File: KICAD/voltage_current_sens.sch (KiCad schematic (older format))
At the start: 4 parts

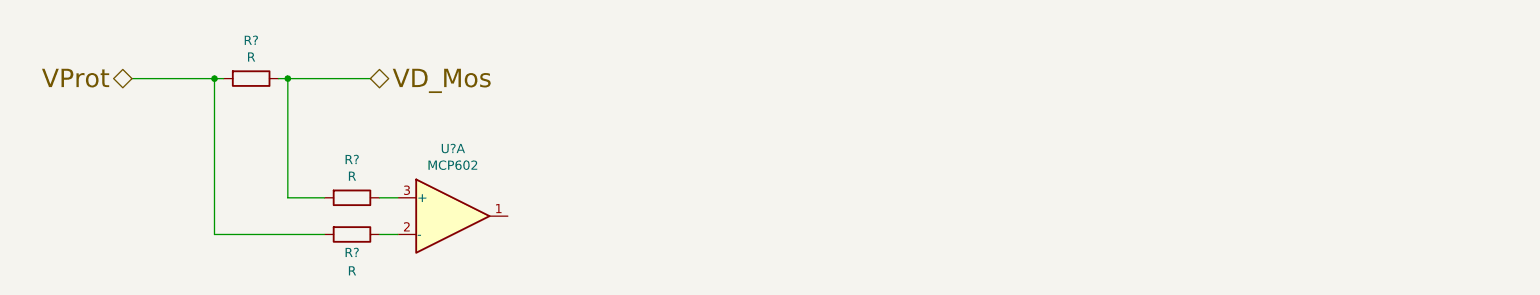
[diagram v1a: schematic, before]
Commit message: labels dans les blocks
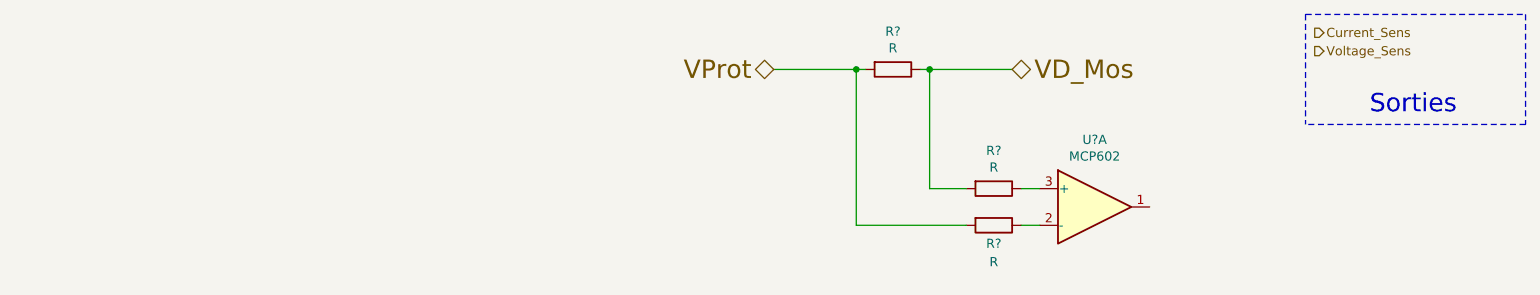
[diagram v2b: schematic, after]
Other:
- note added: "Sorties"
- moved on the sheet: R?, U?A
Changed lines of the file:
@@
 $Descr A4 11693 8268
 encoding utf-8
-Sheet 12 15
+Sheet 3 15
 Title "SESAME"
 Date ""
@@
 Comment4 ""
 $EndDescr
-Text HLabel 3350 3100 2    100  BiDi ~ 0
+Text HLabel 6850 3050 2    100  BiDi ~ 0
 VD_Mos
-Text HLabel 2050 3100 0    100  BiDi ~ 0
+Text HLabel 5550 3050 0    100  BiDi ~ 0
 VProt
 Wire Wire Line
-	2550 3100 2500 3100
+	6050 3050 6000 3050
 Wire Wire Line
-	2850 3100 2900 3100
+	6350 3050 6400 3050
 Wire Wire Line
-	3400 3750 3500 3750
+	6900 3700 7000 3700
 Wire Wire Line
-	3400 3950 3500 3950
+	6900 3900 7000 3900
 Wire Wire Line
-	3100 3750 2900 3750
+	6600 3700 6400 3700
 Wire Wire Line
-	2900 3750 2900 3100
-Connection ~ 2900 3100
+	6400 3700 6400 3050
+Connection ~ 6400 3050
 Wire Wire Line
-	2900 3100 3350 3100
+	6400 3050 6850 3050
 Wire Wire Line
-	2500 3100 2500 3950
+	6000 3050 6000 3900
 Wire Wire Line
-	2500 3950 3100 3950
-Connection ~ 2500 3100
+	6000 3900 6600 3900
+Connection ~ 6000 3050
 Wire Wire Line
-	2500 3100 2050 3100
+	6000 3050 5550 3050
 $Comp
 L Device:R R?
 U 1 1 6109114F
-P 2700 3100
+P 6200 3050
 AR Path="/60F19D5B/6109114F" Ref="R?"  Part="1"
 AR Path="/60F171CE/6109114F" Ref="R?"  Part="1"
-F 0 "R?" V 2493 3100 50  0000 C CNN
-F 1 "R" V 2584 3100 50  0000 C CNN
-F 2 "" V 2630 3100 50  0001 C CNN
-F 3 "~" H 2700 3100 50  0001 C CNN
-	1    2700 3100
+F 0 "R?" V 5993 3050 50  0000 C CNN
+F 1 "R" V 6084 3050 50  0000 C CNN
+F 2 "" V 6130 3050 50  0001 C CNN
+F 3 "~" H 6200 3050 50  0001 C CNN
+	1    6200 3050
 	0    1    1    0
 $EndComp
@@
 L Device:R R?
 U 1 1 61091B7C
-P 3250 3950
+P 6750 3900
 AR Path="/60F19D5B/61091B7C" Ref="R?"  Part="1"
 AR Path="/60F171CE/61091B7C" Ref="R?"  Part="1"
-F 0 "R?" V 3350 3950 50  0000 C CNN
-F 1 "R" V 3450 3950 50  0000 C CNN
-F 2 "" V 3180 3950 50  0001 C CNN
-F 3 "~" H 3250 3950 50  0001 C CNN
-	1    3250 3950
+F 0 "R?" V 6850 3900 50  0000 C CNN
+F 1 "R" V 6950 3900 50  0000 C CNN
+F 2 "" V 6680 3900 50  0001 C CNN
+F 3 "~" H 6750 3900 50  0001 C CNN
+	1    6750 3900
 	0    1    1    0
 $EndComp
@@
 L Device:R R?
 U 1 1 610923D6
-P 3250 3750
+P 6750 3700
 AR Path="/60F19D5B/610923D6" Ref="R?"  Part="1"
 AR Path="/60F171CE/610923D6" Ref="R?"  Part="1"
-F 0 "R?" V 3043 3750 50  0000 C CNN
-F 1 "R" V 3134 3750 50  0000 C CNN
-F 2 "" V 3180 3750 50  0001 C CNN
-F 3 "~" H 3250 3750 50  0001 C CNN
-	1    3250 3750
+F 0 "R?" V 6543 3700 50  0000 C CNN
+F 1 "R" V 6634 3700 50  0000 C CNN
+F 2 "" V 6680 3700 50  0001 C CNN
+F 3 "~" H 6750 3700 50  0001 C CNN
+	1    6750 3700
 	0    1    1    0
 $EndComp
@@
 L Amplifier_Operational:MCP602 U?
 U 1 1 61093F22
-P 3800 3850
+P 7300 3800
 AR Path="/60F19D5B/61093F22" Ref="U?"  Part="1"
 AR Path="/60F171CE/61093F22" Ref="U?"  Part="1"
-F 0 "U?" H 3800 4217 50  0000 C CNN
-F 1 "MCP602" H 3800 4126 50  0000 C CNN
-F 2 "" H 3800 3850 50  0001 C CNN
-F 3 "http://ww1.microchip.com/downloads/en/DeviceDoc/21314g.pdf" H 3800 3850 50  0001 C CNN
-	1    3800 3850
+F 0 "U?" H 7300 4167 50  0000 C CNN
+F 1 "MCP602" H 7300 4076 50  0000 C CNN
+F 2 "" H 7300 3800 50  0001 C CNN
+F 3 "http://ww1.microchip.com/downloads/en/DeviceDoc/21314g.pdf" H 7300 3800 50  0001 C CNN
+	1    7300 3800
 	1    0    0    -1
 $EndComp
+Text HLabel 8500 2850 2    50   Output ~ 0
+Current_Sens
+Text HLabel 8500 2950 2    50   Output ~ 0
+Voltage_Sens
+Wire Notes Line
+	8450 2750 9650 2750
+Wire Notes Line
+	9650 2750 9650 3350
+Wire Notes Line
+	9650 3350 8450 3350
+Wire Notes Line
+	8450 2750 8450 3350
+Text Notes 8800 3300 0    100  ~ 0
+Sorties
 $EndSCHEMATC

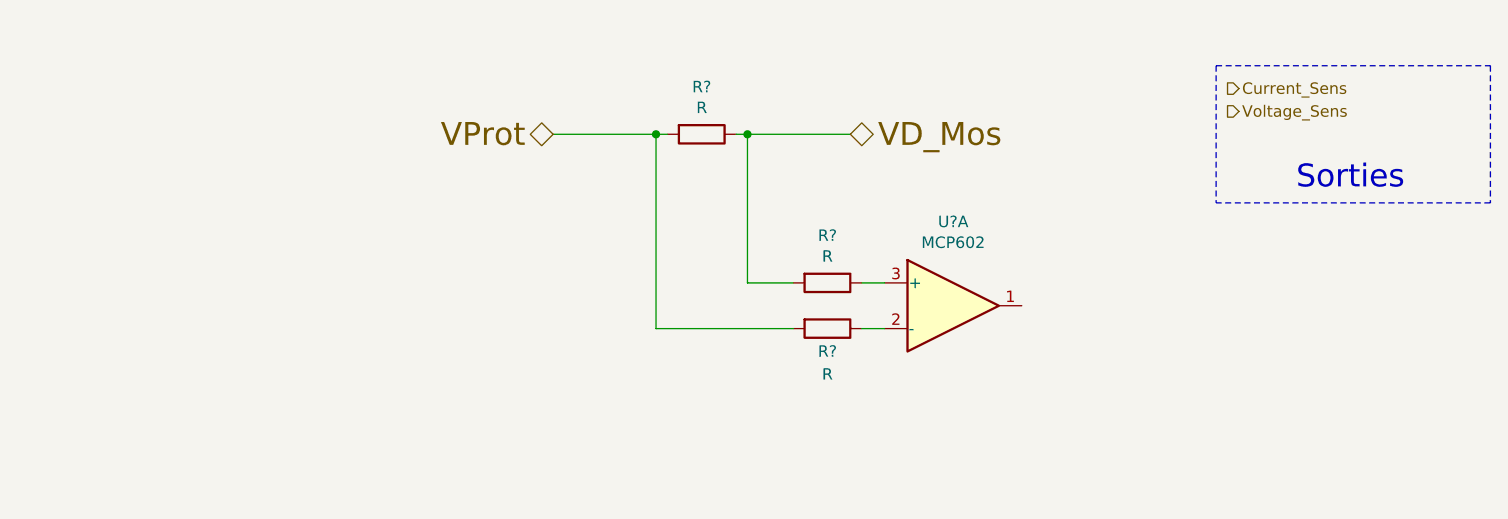
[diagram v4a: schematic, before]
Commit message: added ina240 sim + drawed protect and DC-DC chopper
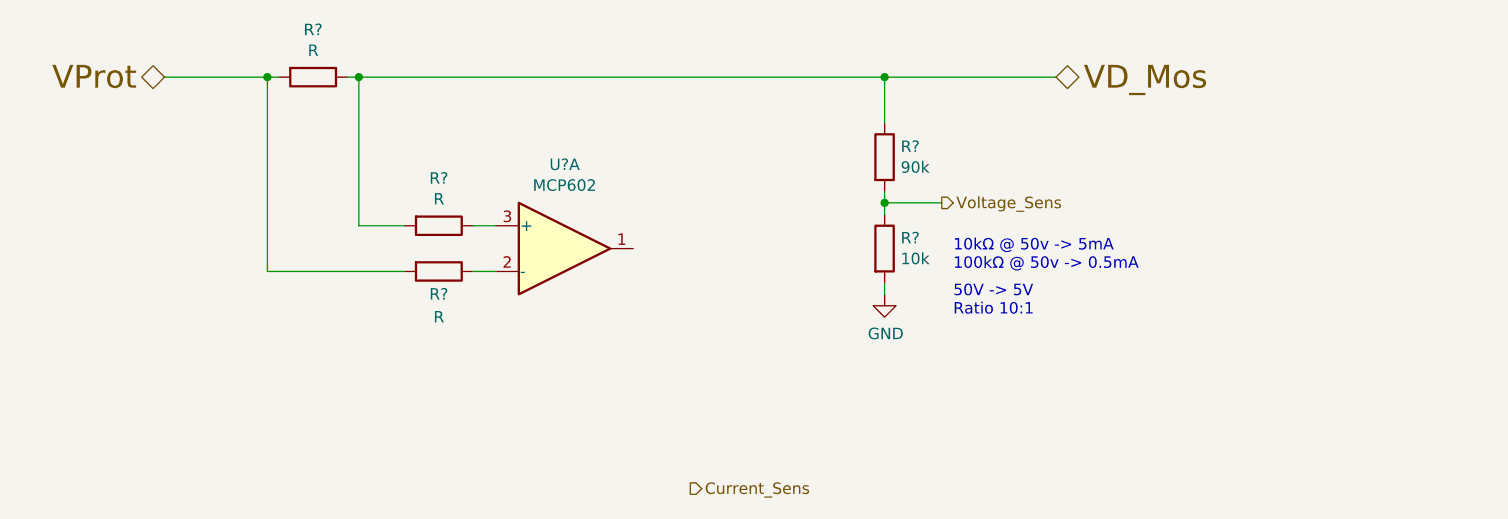
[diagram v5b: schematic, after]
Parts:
- added R?: 90k, symbol Device:R
- added R?: 10k, symbol Device:R
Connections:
- net VD_Mos: now also R?.1
- net Voltage_Sens: now also R?.1, R?.2
- new net GND: R?.2
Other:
- note added: "10kΩ @ 50v -> 5mA\n100kΩ @ 50v -> 0.5mA"
- note added: "50V -> 5V\nRatio 10:1"
- note removed: "Sorties"
- moved on the sheet: R?, U?A
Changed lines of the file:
@@
 Rev ""
 Comp "ALEEA"
-Comment1 ""
+Comment1 "Dessin : Guillaume Arthaud"
 Comment2 ""
 Comment3 ""
 Comment4 ""
 $EndDescr
-Text HLabel 6850 3050 2    100  BiDi ~ 0
+Text HLabel 7750 2800 2    100  BiDi ~ 0
 VD_Mos
-Text HLabel 5550 3050 0    100  BiDi ~ 0
+Text HLabel 3850 2800 0    100  BiDi ~ 0
 VProt
 Wire Wire Line
-	6050 3050 6000 3050
+	4350 2800 4300 2800
 Wire Wire Line
-	6350 3050 6400 3050
+	4650 2800 4700 2800
 Wire Wire Line
-	6900 3700 7000 3700
+	5200 3450 5300 3450
 Wire Wire Line
-	6900 3900 7000 3900
+	5200 3650 5300 3650
 Wire Wire Line
-	6600 3700 6400 3700
+	4900 3450 4700 3450
 Wire Wire Line
-	6400 3700 6400 3050
-Connection ~ 6400 3050
+	4700 3450 4700 2800
+Connection ~ 4700 2800
 Wire Wire Line
-	6400 3050 6850 3050
+	4300 2800 4300 3650
 Wire Wire Line
-	6000 3050 6000 3900
+	4300 3650 4900 3650
+Connection ~ 4300 2800
 Wire Wire Line
-	6000 3900 6600 3900
-Connection ~ 6000 3050
-Wire Wire Line
-	6000 3050 5550 3050
+	4300 2800 3850 2800
 $Comp
 L Device:R R?
 U 1 1 6109114F
-P 6200 3050
+P 4500 2800
 AR Path="/60F19D5B/6109114F" Ref="R?"  Part="1"
 AR Path="/60F171CE/6109114F" Ref="R?"  Part="1"
-F 0 "R?" V 5993 3050 50  0000 C CNN
-F 1 "R" V 6084 3050 50  0000 C CNN
-F 2 "" V 6130 3050 50  0001 C CNN
-F 3 "~" H 6200 3050 50  0001 C CNN
-	1    6200 3050
+F 0 "R?" V 4293 2800 50  0000 C CNN
+F 1 "R" V 4384 2800 50  0000 C CNN
+F 2 "" V 4430 2800 50  0001 C CNN
+F 3 "~" H 4500 2800 50  0001 C CNN
+	1    4500 2800
 	0    1    1    0
 $EndComp
@@
 L Device:R R?
 U 1 1 61091B7C
-P 6750 3900
+P 5050 3650
 AR Path="/60F19D5B/61091B7C" Ref="R?"  Part="1"
 AR Path="/60F171CE/61091B7C" Ref="R?"  Part="1"
-F 0 "R?" V 6850 3900 50  0000 C CNN
-F 1 "R" V 6950 3900 50  0000 C CNN
-F 2 "" V 6680 3900 50  0001 C CNN
-F 3 "~" H 6750 3900 50  0001 C CNN
-	1    6750 3900
+F 0 "R?" V 5150 3650 50  0000 C CNN
+F 1 "R" V 5250 3650 50  0000 C CNN
+F 2 "" V 4980 3650 50  0001 C CNN
+F 3 "~" H 5050 3650 50  0001 C CNN
+	1    5050 3650
 	0    1    1    0
 $EndComp
@@
 L Device:R R?
 U 1 1 610923D6
-P 6750 3700
+P 5050 3450
 AR Path="/60F19D5B/610923D6" Ref="R?"  Part="1"
 AR Path="/60F171CE/610923D6" Ref="R?"  Part="1"
-F 0 "R?" V 6543 3700 50  0000 C CNN
-F 1 "R" V 6634 3700 50  0000 C CNN
-F 2 "" V 6680 3700 50  0001 C CNN
-F 3 "~" H 6750 3700 50  0001 C CNN
-	1    6750 3700
+F 0 "R?" V 4843 3450 50  0000 C CNN
+F 1 "R" V 4934 3450 50  0000 C CNN
+F 2 "" V 4980 3450 50  0001 C CNN
+F 3 "~" H 5050 3450 50  0001 C CNN
+	1    5050 3450
 	0    1    1    0
 $EndComp
@@
 L Amplifier_Operational:MCP602 U?
 U 1 1 61093F22
-P 7300 3800
+P 5600 3550
 AR Path="/60F19D5B/61093F22" Ref="U?"  Part="1"
 AR Path="/60F171CE/61093F22" Ref="U?"  Part="1"
-F 0 "U?" H 7300 4167 50  0000 C CNN
-F 1 "MCP602" H 7300 4076 50  0000 C CNN
-F 2 "" H 7300 3800 50  0001 C CNN
-F 3 "http://ww1.microchip.com/downloads/en/DeviceDoc/21314g.pdf" H 7300 3800 50  0001 C CNN
-	1    7300 3800
+F 0 "U?" H 5600 3917 50  0000 C CNN
+F 1 "MCP602" H 5600 3826 50  0000 C CNN
+F 2 "" H 5600 3550 50  0001 C CNN
+F 3 "http://ww1.microchip.com/downloads/en/DeviceDoc/21314g.pdf" H 5600 3550 50  0001 C CNN
+	1    5600 3550
 	1    0    0    -1
 $EndComp
-Text HLabel 8500 2850 2    50   Output ~ 0
+Text HLabel 6150 4600 2    50   Output ~ 0
 Current_Sens
-Text HLabel 8500 2950 2    50   Output ~ 0
+Text HLabel 7250 3350 2    50   Output ~ 0
 Voltage_Sens
-Wire Notes Line
-	8450 2750 9650 2750
-Wire Notes Line
-	9650 2750 9650 3350
-Wire Notes Line
-	9650 3350 8450 3350
-Wire Notes Line
-	8450 2750 8450 3350
-Text Notes 8800 3300 0    100  ~ 0
-Sorties
+$Comp
+L Device:R R?
+U 1 1 610DBB97
+P 7000 3150
+F 0 "R?" H 7070 3196 50  0000 L CNN
+F 1 "90k" H 7070 3105 50  0000 L CNN
+F 2 "" V 6930 3150 50  0001 C CNN
+F 3 "~" H 7000 3150 50  0001 C CNN
+	1    7000 3150
+	1    0    0    -1
+$EndComp
+$Comp
+L Device:R R?
+U 1 1 610DC636
+P 7000 3550
+F 0 "R?" H 7070 3596 50  0000 L CNN
+F 1 "10k" H 7070 3505 50  0000 L CNN
+F 2 "" V 6930 3550 50  0001 C CNN
+F 3 "~" H 7000 3550 50  0001 C CNN
+	1    7000 3550
+	1    0    0    -1
+$EndComp
+Wire Wire Line
+	7000 3300 7000 3350
+Wire Wire Line
+	7250 3350 7000 3350
+Connection ~ 7000 3350
+Wire Wire Line
+	7000 3350 7000 3400
+Wire Wire Line
+	4700 2800 7000 2800
+Wire Wire Line
+	7000 3000 7000 2800
+Connection ~ 7000 2800
+Wire Wire Line
+	7000 2800 7750 2800
+$Comp
+L power:GND #PWR?
+U 1 1 610DEA27
+P 7000 3750
+F 0 "#PWR?" H 7000 3500 50  0001 C CNN
+F 1 "GND" H 7005 3577 50  0000 C CNN
+F 2 "" H 7000 3750 50  0001 C CNN
+F 3 "" H 7000 3750 50  0001 C CNN
+	1    7000 3750
+	1    0    0    -1
+$EndComp
+Wire Wire Line
+	7000 3750 7000 3700
+Text Notes 7300 3850 0    50   ~ 0
+50V -> 5V\nRatio 10:1
+Text Notes 7300 3650 0    50   ~ 0
+10kΩ @ 50v -> 5mA\n100kΩ @ 50v -> 0.5mA
 $EndSCHEMATC

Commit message: merge program breaker nicolas
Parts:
- added R? (x3): 10k, symbol Device:R
- added R?: R, symbol Device:R
- added U?: MCP602, symbol Amplifier_Operational:MCP602
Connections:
- net GND: now also R?.2
- new net: R?.2, U?.1
- new net: R?.1, R?.2, U?.2 (-)
- new net: R?.1, R?.1, U?.3 (+)
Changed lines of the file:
@@
 $Descr A4 11693 8268
 encoding utf-8
-Sheet 11 15
+Sheet 3 15
 Title "SESAME"
 Date ""
@@
 U 1 1 610DBB97
 P 7000 3150
+AR Path="/60F171CE/610DBB97" Ref="R?"  Part="1"
+AR Path="/60F19D5B/610DBB97" Ref="R?"  Part="1"
 F 0 "R?" H 7070 3196 50  0000 L CNN
 F 1 "90k" H 7070 3105 50  0000 L CNN
@@
 U 1 1 610DC636
 P 7000 3550
+AR Path="/60F171CE/610DC636" Ref="R?"  Part="1"
+AR Path="/60F19D5B/610DC636" Ref="R?"  Part="1"
 F 0 "R?" H 7070 3596 50  0000 L CNN
 F 1 "10k" H 7070 3505 50  0000 L CNN
@@
 U 1 1 610DEA27
 P 7000 3750
+AR Path="/60F171CE/610DEA27" Ref="#PWR?"  Part="1"
+AR Path="/60F19D5B/610DEA27" Ref="#PWR?"  Part="1"
 F 0 "#PWR?" H 7000 3500 50  0001 C CNN
 F 1 "GND" H 7005 3577 50  0000 C CNN
@@
 Text Notes 7300 3650 0    50   ~ 0
 10kΩ @ 50v -> 5mA\n100kΩ @ 50v -> 0.5mA
+$Comp
+L Amplifier_Operational:MCP602 U?
+U 1 1 611928B4
+P 4800 4900
+AR Path="/60F19D5B/611928B4" Ref="U?"  Part="1"
+AR Path="/60F171CE/611928B4" Ref="U?"  Part="1"
+F 0 "U?" H 4800 5267 50  0000 C CNN
+F 1 "MCP602" H 4800 5176 50  0000 C CNN
+F 2 "" H 4800 4900 50  0001 C CNN
+F 3 "http://ww1.microchip.com/downloads/en/DeviceDoc/21314g.pdf" H 4800 4900 50  0001 C CNN
+	1    4800 4900
+	1    0    0    1
+$EndComp
+$Comp
+L Device:R R?
+U 1 1 61192E87
+P 4800 4550
+F 0 "R?" V 5007 4550 50  0000 C CNN
+F 1 "10k" V 4916 4550 50  0000 C CNN
+F 2 "" V 4730 4550 50  0001 C CNN
+F 3 "~" H 4800 4550 50  0001 C CNN
+	1    4800 4550
+	0    -1   -1   0
+$EndComp
+$Comp
+L Device:R R?
+U 1 1 6119509F
+P 4100 4800
+F 0 "R?" V 4307 4800 50  0000 C CNN
+F 1 "10k" V 4216 4800 50  0000 C CNN
+F 2 "" V 4030 4800 50  0001 C CNN
+F 3 "~" H 4100 4800 50  0001 C CNN
+	1    4100 4800
+	0    -1   -1   0
+$EndComp
+$Comp
+L Device:R R?
+U 1 1 61196067
+P 4100 5000
+F 0 "R?" V 4307 5000 50  0000 C CNN
+F 1 "10k" V 4216 5000 50  0000 C CNN
+F 2 "" V 4030 5000 50  0001 C CNN
+F 3 "~" H 4100 5000 50  0001 C CNN
+	1    4100 5000
+	0    1    1    0
+$EndComp
+Wire Wire Line
+	4250 5000 4450 5000
+Wire Wire Line
+	4500 4800 4450 4800
+Wire Wire Line
+	4650 4550 4450 4550
+Wire Wire Line
+	4450 4550 4450 4800
+Connection ~ 4450 4800
+Wire Wire Line
+	4450 4800 4250 4800
+Wire Wire Line
+	4950 4550 5200 4550
+Wire Wire Line
+	5200 4550 5200 4900
+Wire Wire Line
+	5200 4900 5100 4900
+$Comp
+L Device:R R?
+U 1 1 6119C613
+P 4450 5350
+F 0 "R?" H 4520 5396 50  0000 L CNN
+F 1 "R" H 4520 5305 50  0000 L CNN
+F 2 "" V 4380 5350 50  0001 C CNN
+F 3 "~" H 4450 5350 50  0001 C CNN
+	1    4450 5350
+	1    0    0    -1
+$EndComp
+Wire Wire Line
+	4450 5200 4450 5000
+Connection ~ 4450 5000
+Wire Wire Line
+	4450 5000 4500 5000
+$Comp
+L power:GND #PWR?
+U 1 1 611A135F
+P 4450 5500
+F 0 "#PWR?" H 4450 5250 50  0001 C CNN
+F 1 "GND" H 4455 5327 50  0000 C CNN
+F 2 "" H 4450 5500 50  0001 C CNN
+F 3 "" H 4450 5500 50  0001 C CNN
+	1    4450 5500
+	1    0    0    -1
+$EndComp
 $EndSCHEMATC

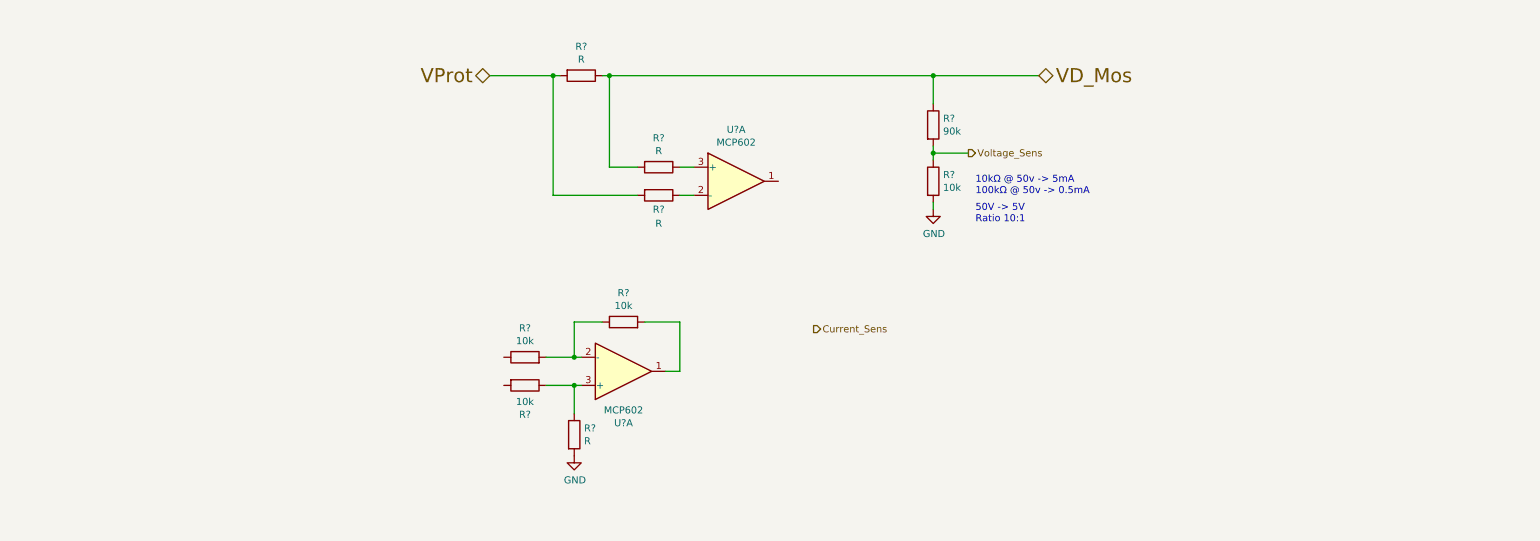
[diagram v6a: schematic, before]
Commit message: mod the main sheet + drawed the first full version of the u/i sensor
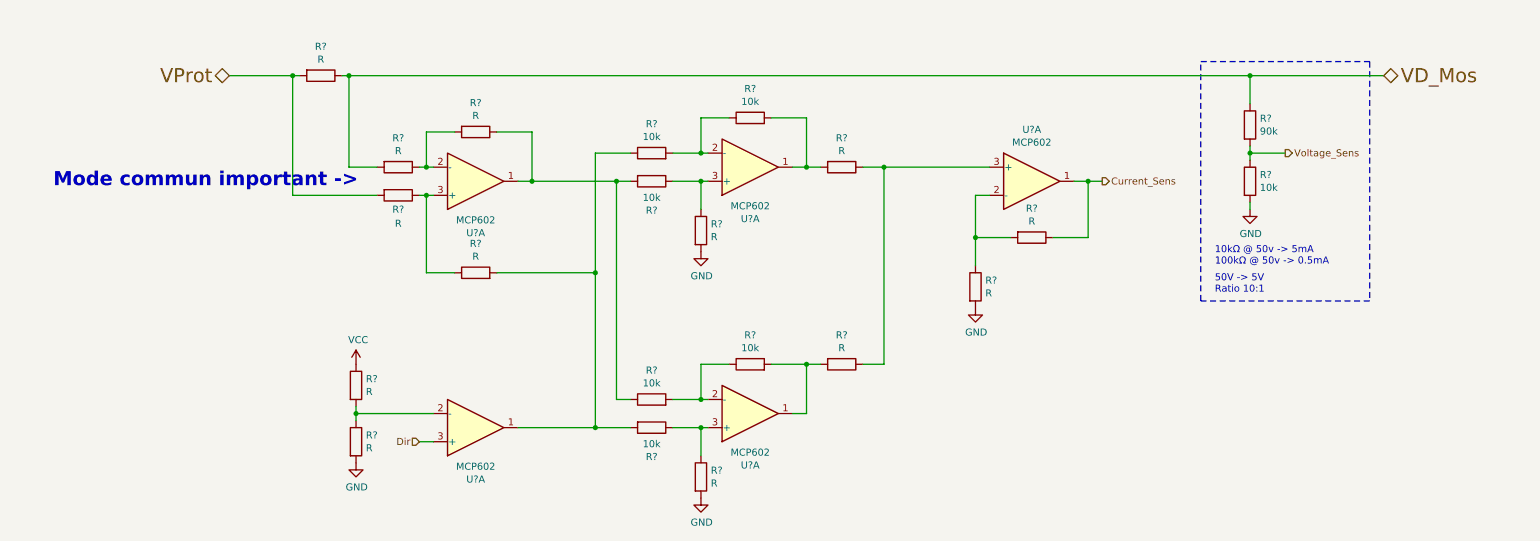
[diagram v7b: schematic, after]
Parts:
- added R? (x9): R, symbol Device:R
- added R? (x3): 10k, symbol Device:R
- added U? (x3): MCP602, symbol Amplifier_Operational:MCP602
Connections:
- net Current_Sens: now also R?.1, U?.1
- net GND: now also R?.2, R?.2, R?.2
- net at R?.1: now also U?.3 (+), R?.1; no longer U?.2 (-)
- net at R?.1: now also U?.2 (-), R?.2; no longer U?.3 (+)
- net at U?.1: now also R?.2, R?.1, R?.1
- net at R?.2, U?.1: now also R?.2
- net at R?.1: now also R?.2, R?.2, U?.1
- new net: R?.2, R?.2, U?.1
- new net: R?.1, R?.2, U?.2 (-) (x3)
- new net: R?.1, R?.1, U?.3 (+) (x2)
- new net Dir: U?.3 (+)
- new net VCC: R?.1
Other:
- note added: "Mode commun important ->"
- moved on the sheet: R?, U?A
